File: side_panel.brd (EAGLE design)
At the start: 81.7 x 112 mm, 47 parts

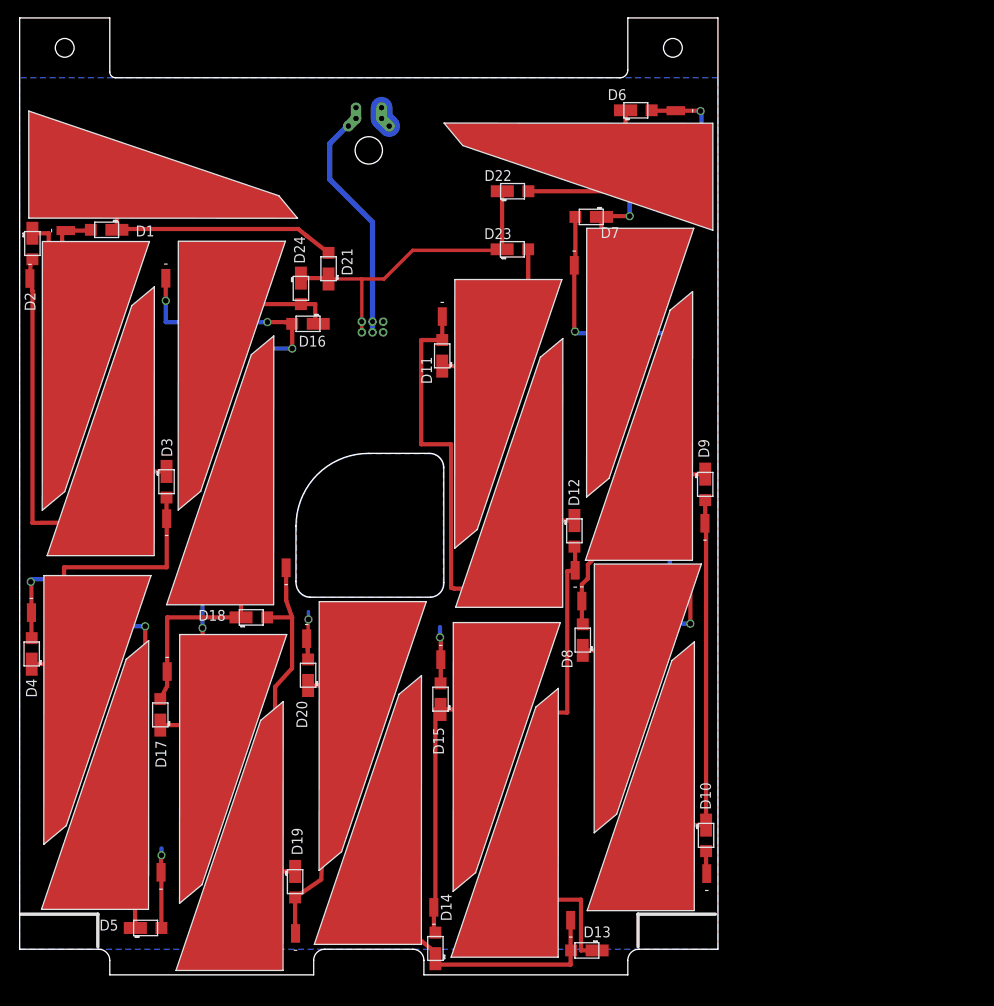
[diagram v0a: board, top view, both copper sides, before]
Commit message: Beginning of new solar panel layout
Changing to pairs of TASC cells to accommodate irregularities in
dimensions
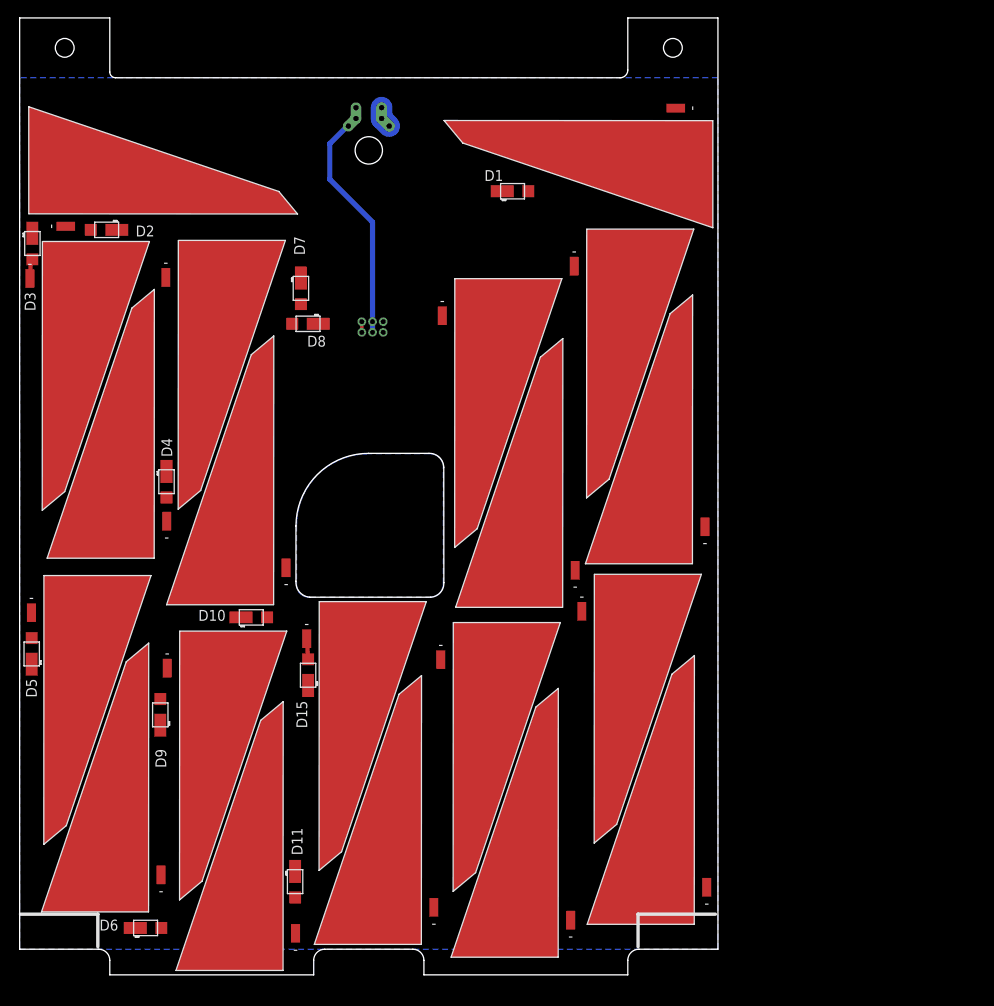
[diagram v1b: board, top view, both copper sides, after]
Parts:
- removed D12, D13, D14, D16, D17, D18, D19, D20, D21, D22, D23, D24: SB_DIODE, phonesat:SB_DIODE
- moved D6 111.6 mm to (14.7, 5.49)
- moved SL7 75.4 mm to (2.97, 39.4)
- moved SL2 74.2 mm to (73.8, 99.8), turned to 270 degrees
- moved SL16 73.3 mm to (46.9, 10.9), turned to 180 degrees
- moved SL13 70.6 mm to (66.5, 80.0), turned to 0 degrees
- moved D9 69.3 mm to (16.5, 30.4), turned to 90 degrees
- moved SL6 65.9 mm to (29.6, 50.6), turned to 180 degrees
- moved SL9 64.0 mm to (18.9, 32.9), turned to 0 degrees
- moved D11 63.9 mm to (32.2, 10.9), turned to 270 degrees
- moved SL5 63.7 mm to (18.7, 78.6), turned to 0 degrees
- moved D10 59.0 mm to (27.1, 41.8), turned to 0 degrees
- moved SL8 58.5 mm to (15.0, 14.7), turned to 180 degrees
- moved SL14 54.7 mm to (78.6, 55.5)
- moved SL18 53.0 mm to (62.9, 9.40)
- moved SL20 49.4 mm to (78.8, 13.2), turned to 180 degrees
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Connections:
- removed net N$1: D11.POS, D12.NEG, SL11.1, SL12.2
- removed net N$11: D10.POS, SL10.1
- removed net N$31: D8.POS, D9.NEG, SL8.1, SL9.2
- removed net N$33: D7.POS, D8.NEG, SL7.1, SL8.2
- removed net N$35: D10.NEG, D9.POS, SL10.2, SL9.1
- removed net N$36: D13.POS, D14.NEG, SL13.1, SL14.2
- removed net N$41: D14.POS, D15.NEG, SL14.1, SL15.2
- removed net N$5: D11.NEG, D23.POS, SL11.2
- removed net N$69: D22.POS, D6.NEG, SL6.2
- removed net N$7: D12.POS, D13.NEG, SL12.1, SL13.2
- removed net N$70: D6.POS, D7.NEG, SL6.1, SL7.2
- net GND: now also D6.POS, SL10.1, SL19.2, SL9.2; no longer D20.POS, D5.POS, SL15.1, SL5.1
- net N$2: now also D8.POS, D9.NEG, SL11.1, SL12.2, SL13.1, SL14.2; no longer D16.POS, D17.NEG, SL16.1, SL17.2
- net N$3: now also D10.NEG, D9.POS, SL13.2, SL14.1, SL15.1, SL16.1; no longer D17.POS, D18.NEG, SL17.1, SL18.2
- net N$37: now also D3.POS, D4.NEG, SL3.1, SL4.2, SL5.1, SL6.2; no longer D2.POS, D3.NEG, SL2.1, SL3.2
- net N$39: now also D4.POS, D5.NEG, SL5.2, SL6.1, SL7.2, SL8.1; no longer D3.POS, D4.NEG, SL3.1, SL4.2
- net N$4: now also D10.POS, D11.NEG, SL15.2, SL16.2, SL17.2; no longer D18.POS, D19.NEG, SL19.2
- net N$45: now also D2.POS, D3.NEG, SL2.1, SL3.2, SL4.1; no longer D1.POS, D2.NEG, SL2.2
- net N$50: now also D5.POS, D6.NEG, SL10.2, SL7.1, SL8.2, SL9.1; no longer D4.POS, D5.NEG, SL4.1, SL5.2
- net N$6: now also D11.POS, D15.NEG, SL17.1, SL18.2; no longer D19.POS, D20.NEG
- net N$8: now also D7.POS, D8.NEG, SL11.2, SL12.1; no longer D16.NEG, D24.POS, SL16.2
- net N$9: now also D1.POS, D2.NEG, SL2.2; no longer D1.NEG, D21.POS
- net V_SOLAR: now also D1.NEG, D7.NEG; no longer D21.NEG, D22.NEG, D23.NEG, D24.NEG
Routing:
- net N$33: track 87.0 -> 0.00 mm, vias 2 -> 0
- net N$2: track 83.8 -> 0.00 mm, vias 4 -> 0
- net N$50: track 63.8 -> 0.30 mm, vias 2 -> 0
- net N$7: track 62.9 -> 0.00 mm
- net N$1: track 60.0 -> 0.00 mm
- net N$4: track 52.5 -> 0.00 mm
- net N$37: track 54.4 -> 2.33 mm
- net N$35: track 49.6 -> 0.00 mm
- net N$6: track 42.2 -> 0.00 mm
- net N$41: track 38.6 -> 0.00 mm
- net N$9: track 37.5 -> 0.00 mm
- net V_SOLAR: track 38.2 -> 1.27 mm
- net N$39: track 36.7 -> 0.00 mm
- net N$70: track 33.9 -> 0.00 mm, vias 2 -> 0
- net N$31: track 30.0 -> 0.00 mm
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
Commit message: New side panel layout
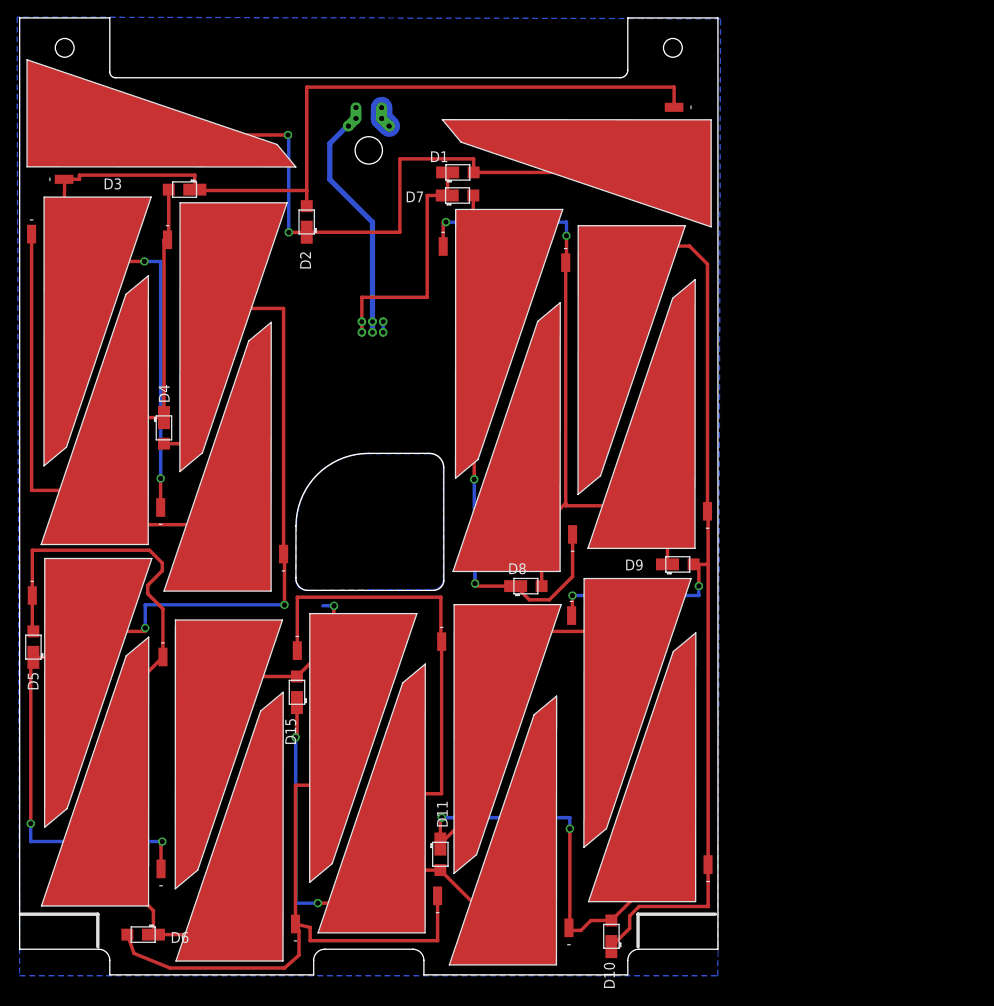
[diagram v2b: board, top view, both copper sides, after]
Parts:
- moved D9 63.1 mm to (77.0, 48.0), turned to 0 degrees
- moved D10 56.3 mm to (69.3, 4.51), turned to 90 degrees
- moved D8 39.9 mm to (59.2, 45.5), turned to 0 degrees
- moved SL19 33.6 mm to (34.1, 35.0)
- moved SL16 32.5 mm to (79.0, 15.9)
- moved SL20 31.5 mm to (47.3, 12.2)
- moved SL15 31.1 mm to (66.2, 39.0)
- moved D2 23.4 mm to (33.6, 88.1), turned to 90 degrees
- moved D7 21.3 mm to (51.2, 91.2), turned to 0 degrees
- moved D3 18.9 mm to (19.3, 91.9), turned to 180 degrees
- moved D11 17.3 mm to (49.2, 14.1)
- moved SL11 8.10 mm to (51.2, 82.2)
- moved D1 6.77 mm to (51.3, 93.9)
- moved D4 6.31 mm to (16.9, 64.0)
- moved SL1 5.50 mm to (8.20, 94.7)
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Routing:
- net N$39: track 0.00 -> 163.3 mm, vias 0 -> 4
- net N$45: track 0.00 -> 139.8 mm, vias 0 -> 2
- net N$3: track 0.00 -> 126.3 mm, vias 0 -> 2
- net N$6: track 0.00 -> 120.9 mm, vias 0 -> 2
- net GND: track 4.26 -> 117.2 mm, vias 0 -> 1
- net N$37: track 2.33 -> 105.8 mm
- net N$9: track 0.00 -> 102.3 mm, vias 0 -> 2
- net N$4: track 0.00 -> 92.7 mm, vias 0 -> 2
- net N$50: track 0.30 -> 86.2 mm
- net N$2: track 0.00 -> 82.2 mm, vias 0 -> 2
- net N$8: track 0.97 -> 64.0 mm, vias 0 -> 2
- net V_SOLAR: track 1.27 -> 28.8 mm
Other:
- outline, holes or cut-outs redrawn

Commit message: Revert 959c034..d13c0e4
This rolls back to commit 959c03423f2cbd105642679eef46985d8f87b8b7.
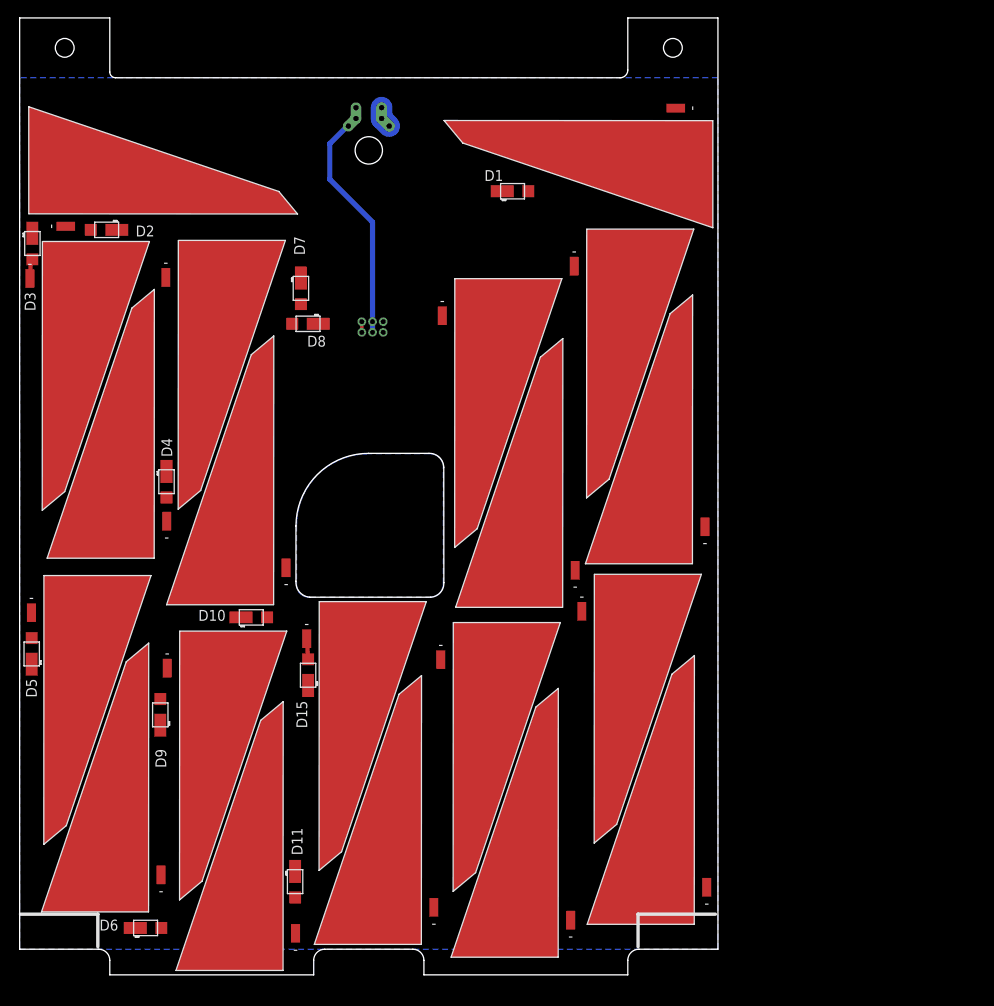
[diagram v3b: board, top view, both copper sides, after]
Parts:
- moved D9 63.1 mm to (16.5, 30.4), turned to 90 degrees
- moved D10 56.3 mm to (27.1, 41.8), turned to 0 degrees
- moved D8 39.9 mm to (33.8, 76.2), turned to 180 degrees
- moved SL19 33.6 mm to (67.4, 39.5)
- moved SL16 32.5 mm to (46.9, 10.9)
- moved SL20 31.5 mm to (78.8, 13.2)
- moved SL15 31.1 mm to (35.2, 36.4)
- moved D2 23.4 mm to (10.2, 87.2), turned to 180 degrees
- moved D7 21.3 mm to (32.9, 80.3), turned to 270 degrees
- moved D3 18.9 mm to (1.49, 85.6), turned to 270 degrees
- moved D11 17.3 mm to (32.2, 10.9)
- moved SL11 8.10 mm to (51.1, 74.2)
- moved D1 6.77 mm to (57.7, 91.7)
- moved D4 6.31 mm to (17.2, 57.7)
- moved SL1 5.50 mm to (8.40, 89.2)
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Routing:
- net N$39: track 163.3 -> 0.00 mm, vias 4 -> 0
- net N$45: track 139.8 -> 0.00 mm, vias 2 -> 0
- net N$3: track 126.3 -> 0.00 mm, vias 2 -> 0
- net N$6: track 120.9 -> 0.00 mm, vias 2 -> 0
- net GND: track 117.2 -> 4.26 mm, vias 1 -> 0
- net N$37: track 105.8 -> 2.33 mm
- net N$9: track 102.3 -> 0.00 mm, vias 2 -> 0
- net N$4: track 92.7 -> 0.00 mm, vias 2 -> 0
- net N$50: track 86.2 -> 0.30 mm
- net N$2: track 82.2 -> 0.00 mm, vias 2 -> 0
- net N$8: track 64.0 -> 0.97 mm, vias 2 -> 0
- net V_SOLAR: track 28.8 -> 1.27 mm
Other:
- outline, holes or cut-outs redrawn

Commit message: Fixed some schematic + layout issues on solar panel
This reverts commit 959c03423f2cbd105642679eef46985d8f87b8b7.

Conflicts:
	side_panel.brd
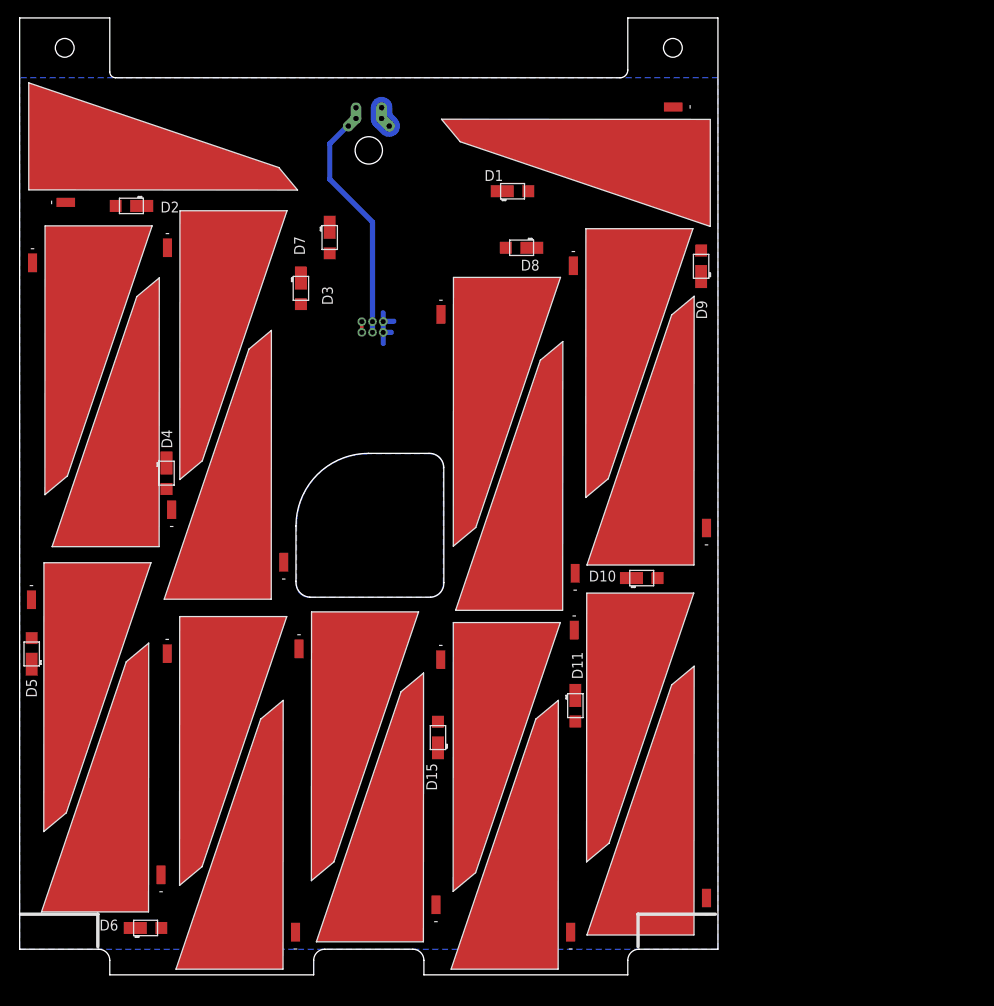
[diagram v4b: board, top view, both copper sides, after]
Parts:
- moved D9 82.2 mm to (79.8, 82.9)
- moved D10 45.9 mm to (72.8, 46.4)
- moved D11 38.7 mm to (65.0, 31.5)
- moved D3 34.8 mm to (36.3, 86.3)
- moved SL19 33.4 mm to (34.3, 35.1)
- moved SL16 31.9 mm to (78.8, 12.0)
- moved SL20 31.8 mm to (47.1, 11.2)
- moved SL15 31.3 mm to (66.5, 37.4)
- moved D8 26.5 mm to (58.8, 85.1)
- moved D15 16.9 mm to (49.0, 27.8)
- moved SL3 16.5 mm to (18.9, 82.1)
- moved SL5 15.7 mm to (3.10, 80.3)
- moved SL6 15.0 mm to (16.2, 57.5)
- moved SL4 14.5 mm to (29.3, 51.3)
- moved D2 4.03 mm to (13.1, 90.0)
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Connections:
- net GND: now also SL19.1, SL9.1; no longer SL19.2, SL9.2
- net N$2: now also SL12.1, SL13.2; no longer SL12.2, SL13.1
- net N$3: now also SL13.1, SL15.2, SL16.2; no longer SL13.2, SL15.1, SL16.1
- net N$37: now also SL4.1, SL5.2; no longer SL4.2, SL5.1
- net N$39: now also SL5.1, SL8.2; no longer SL5.2, SL8.1
- net N$4: now also SL15.1, SL16.1, SL18.2; no longer SL15.2, SL16.2, SL18.1
- net N$45: now also SL4.2; no longer SL4.1
- net N$50: now also SL8.1, SL9.2; no longer SL8.2, SL9.1
- net N$6: now also SL18.1, SL19.2; no longer SL18.2, SL19.1
- net N$8: now also SL12.2; no longer SL12.1
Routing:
- net N$7: track 0.00 -> 3.60 mm
- net N$37: track 2.33 -> 0.00 mm
- net GND: track 4.26 -> 2.53 mm
- net N$5: track 0.00 -> 1.30 mm
- net N$8: track 0.97 -> 0.00 mm
- net N$1: track 0.00 -> 0.90 mm

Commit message: Finished solar panel layout
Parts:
- removed D15: SB_DIODE, phonesat:SB_DIODE
- added D12: SB_DIODE, phonesat:SB_DIODE
- moved SL2 96.2 mm to (102.5, 8.23), turned to 180 degrees
- moved U$2 85.8 mm to (101.5, 39.4), turned to 180 degrees
- moved U$4 85.8 mm to (101.5, 42.4), turned to 0 degrees
- moved SL1 85.7 mm to (92.0, 73.3), turned to 0 degrees
- moved D2 84.2 mm to (86.5, 48.6)
- moved SL5 77.8 mm to (80.8, 78.4), turned to 270 degrees
- moved D10 67.2 mm to (12.6, 16.7), turned to 180 degrees
- moved SL3 66.4 mm to (82.4, 62.8), turned to 270 degrees
- moved SL13 66.2 mm to (81.6, 15.6), turned to 270 degrees
- moved SL16 64.1 mm to (15.3, 2.93), turned to 90 degrees
- moved D9 60.0 mm to (86.0, 23.3), turned to 270 degrees
- moved D6 59.8 mm to (5.99, 64.6), turned to 180 degrees
- moved SL14 56.4 mm to (57.8, 2.93), turned to 90 degrees
- moved D1 56.3 mm to (83.5, 41.6)
- moved SL18 55.5 mm to (8.50, 18.8), turned to 90 degrees
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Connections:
- net GND: now also D12.POS; no longer D15.POS
- net N$6: now also D12.NEG; no longer D15.NEG
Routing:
- net N$45: track 0.00 -> 148.7 mm, vias 0 -> 2
- net N$39: track 0.00 -> 121.1 mm, vias 0 -> 3
- net N$3: track 0.00 -> 116.1 mm, vias 0 -> 2
- net N$6: track 0.00 -> 100.1 mm, vias 0 -> 2
- net N$4: track 0.00 -> 98.8 mm, vias 0 -> 2
- net N$37: track 0.00 -> 98.1 mm, vias 0 -> 2
- net N$50: track 0.30 -> 94.5 mm
- net N$9: track 0.00 -> 86.7 mm
- net N$2: track 0.00 -> 85.4 mm
- net N$8: track 0.00 -> 60.7 mm
- net GND: track 2.53 -> 27.8 mm, vias 0 -> 5
- net V_SOLAR: track 1.27 -> 13.8 mm
- net N$7: track 3.60 -> 0.00 mm
- net N$5: track 1.30 -> 0.00 mm
- net N$1: track 0.90 -> 0.00 mm
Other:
- board size 81.7 x 112 mm -> 112 x 81.7 mm
- board text added: "Side Solar Panel V1.1"
